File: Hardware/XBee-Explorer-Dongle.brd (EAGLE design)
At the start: 40.6 x 27.9 mm, 37 parts, among them U2 XBEE-1B3, U3 MIC5219 3.3V, U4 FTS31XS-U

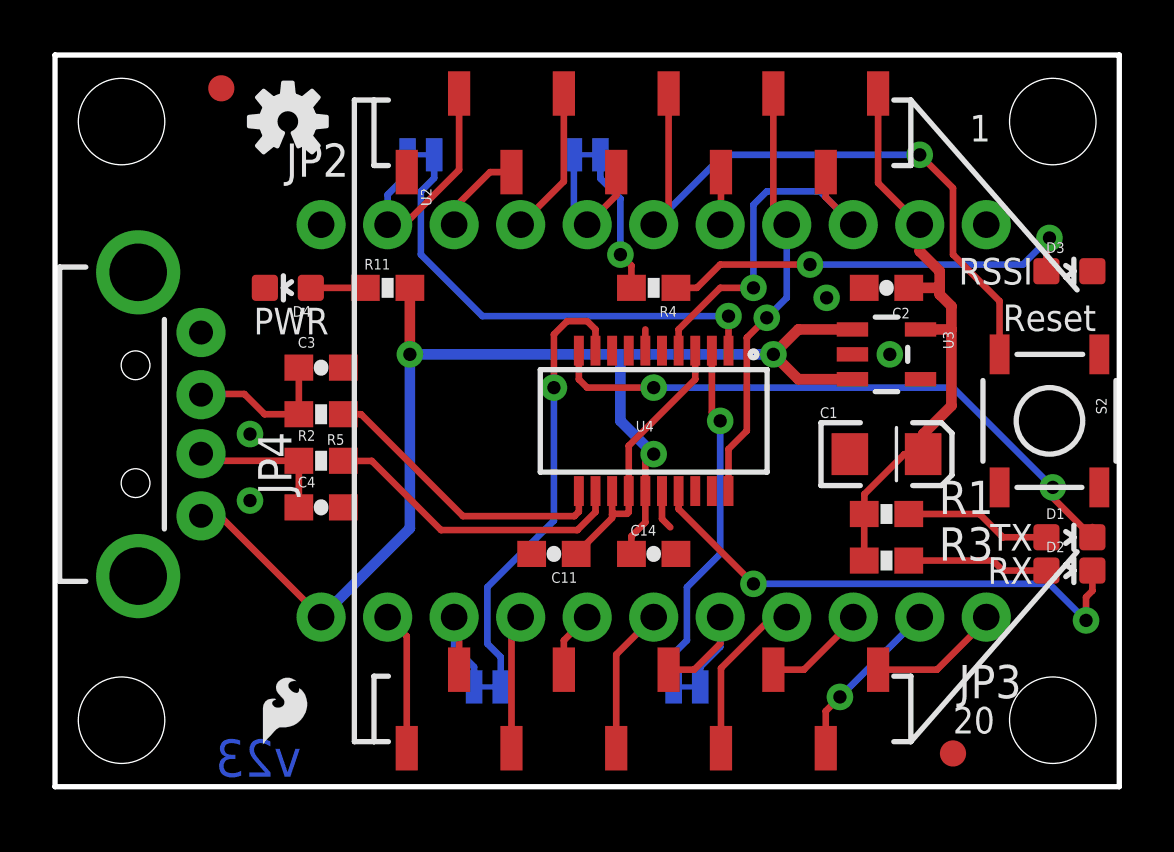
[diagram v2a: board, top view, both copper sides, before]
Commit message: Fixed qc issues.
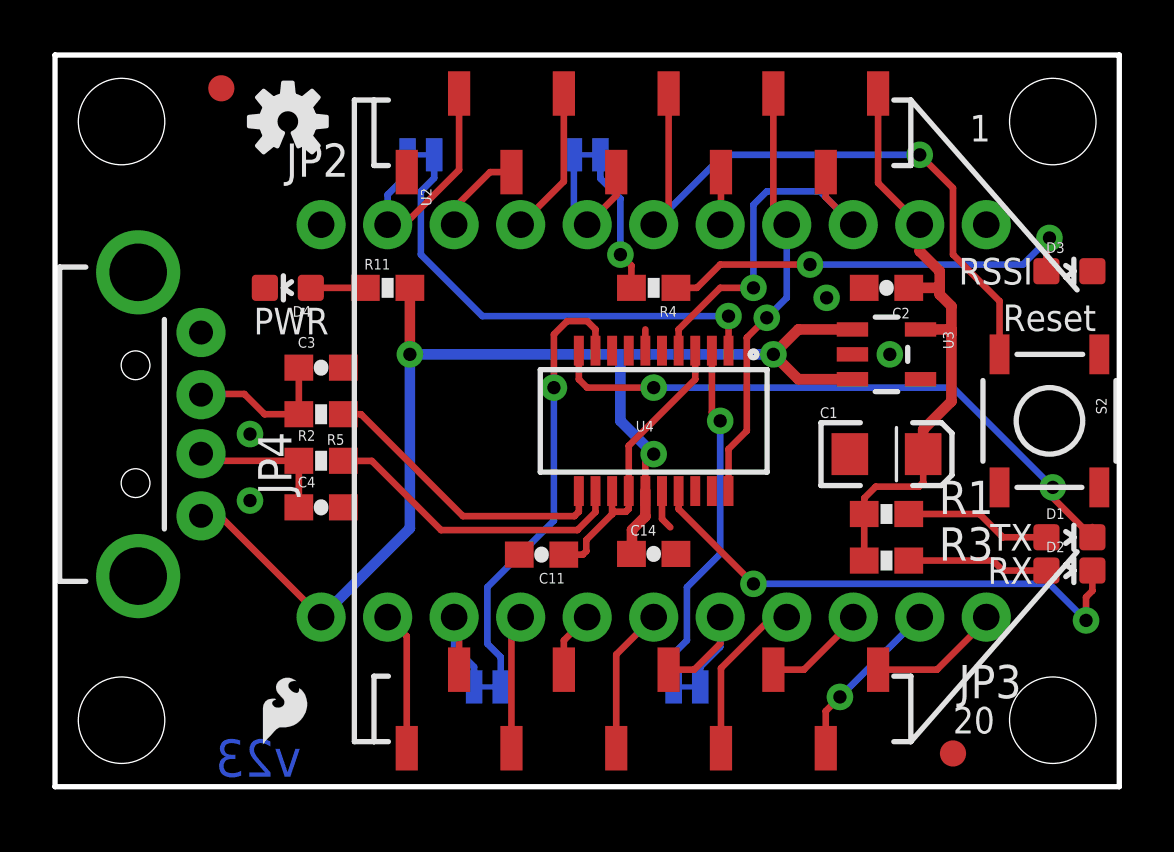
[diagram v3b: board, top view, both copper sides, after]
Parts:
- moved C11 0.47 mm to (18.6, 8.86)
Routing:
- net 3.3V: track 23.3 -> 23.9 mm
- net 3V-INT: track 10.9 -> 11.4 mm
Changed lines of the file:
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@@
 <layer number="23" name="tOrigins" color="15" fill="1" visible="yes" active="yes"/>
 <layer number="24" name="bOrigins" color="15" fill="1" visible="yes" active="yes"/>
-<layer number="25" name="tNames" color="7" fill="1" visible="no" active="yes"/>
-<layer number="26" name="bNames" color="7" fill="1" visible="no" active="yes"/>
-<layer number="27" name="tValues" color="7" fill="1" visible="no" active="yes"/>
-<layer number="28" name="bValues" color="7" fill="1" visible="no" active="yes"/>
+<layer number="25" name="tNames" color="7" fill="1" visible="yes" active="yes"/>
+<layer number="26" name="bNames" color="7" fill="1" visible="yes" active="yes"/>
+<layer number="27" name="tValues" color="7" fill="1" visible="yes" active="yes"/>
+<layer number="28" name="bValues" color="7" fill="1" visible="yes" active="yes"/>
 <layer number="29" name="tStop" color="7" fill="3" visible="no" active="yes"/>
 <layer number="30" name="bStop" color="7" fill="6" visible="no" active="yes"/>
 <layer number="31" name="tCream" color="7" fill="4" visible="no" active="yes"/>
 <layer number="32" name="bCream" color="7" fill="5" visible="no" active="yes"/>
-<layer number="33" name="tFinish" color="6" fill="3" visible="no" active="yes"/>
-<layer number="34" name="bFinish" color="6" fill="6" visible="no" active="yes"/>
-<layer number="35" name="tGlue" color="7" fill="4" visible="no" active="yes"/>
-<layer number="36" name="bGlue" color="7" fill="5" visible="no" active="yes"/>
-<layer number="37" name="tTest" color="7" fill="1" visible="no" active="yes"/>
-<layer number="38" name="bTest" color="7" fill="1" visible="no" active="yes"/>
+<layer number="33" name="tFinish" color="6" fill="3" visible="yes" active="yes"/>
+<layer number="34" name="bFinish" color="6" fill="6" visible="yes" active="yes"/>
+<layer number="35" name="tGlue" color="7" fill="4" visible="yes" active="yes"/>
+<layer number="36" name="bGlue" color="7" fill="5" visible="yes" active="yes"/>
+<layer number="37" name="tTest" color="7" fill="1" visible="yes" active="yes"/>
+<layer number="38" name="bTest" color="7" fill="1" visible="yes" active="yes"/>
 <layer number="39" name="tKeepout" color="4" fill="11" visible="yes" active="yes"/>
 <layer number="40" name="bKeepout" color="1" fill="11" visible="yes" active="yes"/>
@@
 </autorouter>
 <elements>
-<element name="C11" library="SparkFun-Capacitors" package="0603-CAP" value="0.1uF" x="19.05" y="8.89" smashed="yes" rot="R180">
-<attribute name="NAME" x="19.939" y="8.1915" size="0.4064" layer="25" rot="R180"/>
-<attribute name="VALUE" value="0.1uF" x="16.1925" y="8.763" size="0.4064" layer="27"/>
-<attribute name="PROD_ID" value="CAP-00810" x="19.05" y="8.89" size="1.778" layer="27" rot="R180" display="off"/>
+<element name="C11" library="SparkFun-Capacitors" package="0603-CAP" value="0.1uF" x="18.5775625" y="8.862059375" smashed="yes" rot="R180">
+<attribute name="NAME" x="19.4665625" y="8.163559375" size="0.4064" layer="25" rot="R180"/>
+<attribute name="VALUE" value="0.1uF" x="15.7200625" y="8.735059375" size="0.4064" layer="27"/>
+<attribute name="PROD_ID" value="CAP-00810" x="18.5775625" y="8.862059375" size="1.778" layer="27" rot="R180" display="off"/>
 </element>
 <element name="R11" library="SparkFun-Resistors" package="0603-RES" value="1K" x="12.7" y="19.05" smashed="yes">
@@
 <contactref element="JP3" pad="11"/>
 <contactref element="U4" pad="15"/>
-<wire x1="22.01" y1="8.89" x2="22.01" y2="9.564" width="0.254" layer="1"/>
-<wire x1="22.01" y1="9.564" x2="22.5425" y2="10.0965" width="0.254" layer="1"/>
-<wire x1="22.5425" y1="11.2903" x2="22.5425" y2="10.0965" width="0.254" layer="1"/>
 <wire x1="13.55" y1="19.05" x2="13.55" y2="16.51" width="0.4064" layer="1"/>
 <via x="13.55" y="16.51" extent="1-16" drill="0.508"/>
@@
 <wire x1="5.575" y1="10.343" x2="6.294" y2="10.343" width="0.254" layer="1"/>
 <wire x1="6.294" y1="10.343" x2="10.16" y2="6.477" width="0.254" layer="1"/>
+<wire x1="22.5425" y1="11.2903" x2="22.5425" y2="10.320021875" width="0.4064" layer="1"/>
+<wire x1="22.5425" y1="10.320021875" x2="22.031959375" y2="9.80948125" width="0.4064" layer="1"/>
+<wire x1="22.031959375" y1="9.80948125" x2="22.031959375" y2="8.911959375" width="0.4064" layer="1"/>
+<wire x1="22.031959375" y1="8.911959375" x2="22.01" y2="8.89" width="0.4064" layer="1"/>
 </signal>
 <signal name="N$38">
@@
 <wire x1="30.9" y1="10.414" x2="30.9" y2="8.636" width="0.254" layer="1"/>
 <wire x1="30.9" y1="10.414" x2="30.9" y2="10.58" width="0.254" layer="1"/>
-<wire x1="33.15" y1="12.7" x2="33.15" y2="13.465" width="0.4064" layer="1"/>
-<wire x1="33.15" y1="13.465" x2="34.229" y2="14.544" width="0.4064" layer="1"/>
-<wire x1="33.0501" y1="17.46" x2="34.229" y2="17.46" width="0.4064" layer="1"/>
+<wire x1="33.0501" y1="17.46" x2="34.07918125" y2="17.46" width="0.4064" layer="1"/>
+<wire x1="34.07918125" y1="17.46" x2="34.229" y2="17.46" width="0.4064" layer="1"/>
 <wire x1="33.02" y1="21.463" x2="33.02" y2="20.447" width="0.4064" layer="1"/>
 <wire x1="33.02" y1="20.447" x2="33.782" y2="19.685" width="0.4064" layer="1"/>
@@
 <wire x1="34.229" y1="17.46" x2="34.229" y2="18.349" width="0.4064" layer="1"/>
 <wire x1="32.6" y1="19.05" x2="33.782" y2="19.05" width="0.4064" layer="1"/>
-<wire x1="34.229" y1="17.46" x2="34.229" y2="14.544" width="0.4064" layer="1"/>
 <contactref element="U2" pad="1"/>
-<wire x1="33.15" y1="12.7" x2="32.4358" y2="12.7" width="0.254" layer="1"/>
-<wire x1="32.4358" y1="12.7" x2="30.90671875" y2="11.17091875" width="0.254" layer="1"/>
-<wire x1="30.90671875" y1="11.17091875" x2="30.90671875" y2="10.42071875" width="0.254" layer="1"/>
 <wire x1="30.90671875" y1="10.42071875" x2="30.9" y2="10.414" width="0.254" layer="1"/>
+<wire x1="33.15" y1="12.7" x2="33.15" y2="13.635178125" width="0.4064" layer="1"/>
+<wire x1="33.15" y1="13.635178125" x2="34.229040625" y2="14.71421875" width="0.4064" layer="1"/>
+<wire x1="34.229040625" y1="14.71421875" x2="34.229040625" y2="17.310140625" width="0.4064" layer="1"/>
+<wire x1="34.229040625" y1="17.310140625" x2="34.07918125" y2="17.46" width="0.4064" layer="1"/>
+<wire x1="30.90671875" y1="10.42071875" x2="30.90671875" y2="11.0236" width="0.254" layer="1"/>
+<wire x1="30.90671875" y1="11.0236" x2="31.341059375" y2="11.457940625" width="0.254" layer="1"/>
+<wire x1="31.341059375" y1="11.457940625" x2="32.989521875" y2="11.457940625" width="0.254" layer="1"/>
+<wire x1="32.989521875" y1="11.457940625" x2="33.15208125" y2="11.6205" width="0.254" layer="1"/>
+<wire x1="33.15208125" y1="11.6205" x2="33.15208125" y2="12.69791875" width="0.254" layer="1"/>
+<wire x1="33.15208125" y1="12.69791875" x2="33.15" y2="12.7" width="0.254" layer="1"/>
 </signal>
 <signal name="TXLED">
@@
 <wire x1="24.4475" y1="16.6497" x2="24.4475" y2="15.5575" width="0.254" layer="1"/>
 <wire x1="24.4475" y1="15.5575" x2="21.9075" y2="13.0175" width="0.254" layer="1"/>
-<wire x1="21.2725" y1="11.2903" x2="21.2725" y2="10.398759375" width="0.254" layer="1"/>
-<wire x1="21.2725" y1="10.398759375" x2="21.2725" y2="10.2625" width="0.254" layer="1"/>
-<wire x1="21.2725" y1="10.2625" x2="19.9" y2="8.89" width="0.254" layer="1"/>
-<wire x1="21.9075" y1="11.2903" x2="21.9075" y2="10.482578125" width="0.254" layer="1"/>
-<wire x1="21.9075" y1="10.482578125" x2="21.846540625" y2="10.42161875" width="0.254" layer="1"/>
-<wire x1="21.846540625" y1="10.42161875" x2="21.295359375" y2="10.42161875" width="0.254" layer="1"/>
-<wire x1="21.295359375" y1="10.42161875" x2="21.2725" y2="10.398759375" width="0.254" layer="1"/>
+<wire x1="20.152359375" y1="8.862059375" x2="20.28698125" y2="8.99668125" width="0.254" layer="1"/>
+<wire x1="20.28698125" y1="8.99668125" x2="20.28698125" y2="9.423403125" width="0.254" layer="1"/>
+<wire x1="20.28698125" y1="9.423403125" x2="21.269959375" y2="10.40638125" width="0.254" layer="1"/>
+<wire x1="21.269959375" y1="10.40638125" x2="21.269959375" y2="11.287759375" width="0.254" layer="1"/>
+<wire x1="21.269959375" y1="11.287759375" x2="21.2725" y2="11.2903" width="0.254" layer="1"/>
+<wire x1="21.9075" y1="11.2903" x2="21.9075" y2="10.607040625" width="0.254" layer="1"/>
+<wire x1="21.9075" y1="10.607040625" x2="21.80081875" y2="10.500359375" width="0.254" layer="1"/>
+<wire x1="21.80081875" y1="10.500359375" x2="21.3639375" y2="10.500359375" width="0.254" layer="1"/>
+<wire x1="21.3639375" y1="10.500359375" x2="21.269959375" y2="10.40638125" width="0.254" layer="1"/>
+<wire x1="20.152359375" y1="8.862059375" x2="19.4275625" y2="8.862059375" width="0.254" layer="1"/>
 </signal>
 <signal name="N$3">
